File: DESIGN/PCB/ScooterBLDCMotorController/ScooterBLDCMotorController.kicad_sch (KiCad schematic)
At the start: 30 parts, among them J1 M1 OUTPUT, J10 RC_ENABLE, J2 M1 INPUT, J3 M2 INPUT, J4 M2 OUTPUT, J5 I2C, J6 TEST SWITCH, J7 RC CH 1, J8 RC CH 2, J9 RC_PWR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

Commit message: Latest PCB and Rev1.0 release
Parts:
- removed J2: M1 INPUT, Connector_JST:JST_XH_B3B-XH-A_1x03_P2.50mm_Vertical, symbol Connector_Generic:Conn_01x03
- removed J3: M2 INPUT, Connector_JST:JST_XH_B3B-XH-A_1x03_P2.50mm_Vertical, symbol Connector_Generic:Conn_01x03
- added J11: TO M2 ENCODER, Connector_JST:JST_XH_B5B-XH-A_1x05_P2.50mm_Vertical, symbol Connector_Generic:Conn_01x05
- added J12: M2 INPUT, Connector_JST:JST_XH_B5B-XH-A_1x05_P2.50mm_Vertical, symbol Connector_Generic:Conn_01x05
- added J2: TO M1 ENCODER, Connector_JST:JST_XH_B5B-XH-A_1x05_P2.50mm_Vertical, symbol Connector_Generic:Conn_01x05
- added J3: M1 INPUT, Connector_JST:JST_XH_B5B-XH-A_1x05_P2.50mm_Vertical, symbol Connector_Generic:Conn_01x05
- R1: footprint Resistor_THT:R_Axial_DIN0204_L3.6mm_D1.6mm_P5.08mm_Vertical -> Resistor_THT:R_Axial_DIN0204_L3.6mm_D1.6mm_P7.62mm_Horizontal
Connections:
- net M1 B: now also J2.3 (Pin_3), J3.3 (Pin_3)
- net M1 G: now also J2.4 (Pin_4), J3.4 (Pin_4)
- net M1 Y: now also J2.2 (Pin_2), J3.2 (Pin_2)
- net M2 B: now also J11.3 (Pin_3), J12.3 (Pin_3)
- net M2 G: now also J11.4 (Pin_4), J12.4 (Pin_4)
- net M2 Y: now also J11.2 (Pin_2), J12.2 (Pin_2)
- new net: J11.1 (Pin_1), J12.1 (Pin_1)
- new net: J11.5 (Pin_5), J12.5 (Pin_5)
- new net: J2.1 (Pin_1), J3.1 (Pin_1)
- new net: J2.5 (Pin_5), J3.5 (Pin_5)
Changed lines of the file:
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@@
   (junction (at 71.12 177.8) (diameter 0) (color 0 0 0 0)
   )
+  (junction (at 71.12 181.61) (diameter 0) (color 0 0 0 0)
+  )
   (junction (at 109.22 167.64) (diameter 0) (color 0 0 0 0)
   )
@@
   (junction (at 106.68 172.72) (diameter 0) (color 0 0 0 0)
   )
+  (junction (at 104.14 181.61) (diameter 0) (color 0 0 0 0)
+  )
+  (junction (at 73.66 181.61) (diameter 0) (color 0 0 0 0)
+  )
+  (junction (at 76.2 181.61) (diameter 0) (color 0 0 0 0)
+  )
   (junction (at 203.2 96.52) (diameter 0) (color 0 0 0 0)
   )
   (junction (at 104.14 177.8) (diameter 0) (color 0 0 0 0)
   )
+  (junction (at 106.68 181.61) (diameter 0) (color 0 0 0 0)
+  )
+  (junction (at 109.22 181.61) (diameter 0) (color 0 0 0 0)
+  )
   (wire (pts (xy 85.09 140.97) (xy 81.28 140.97))
     (stroke (width 0) (type default) (color 0 0 0 0))
@@
     (stroke (width 0) (type default) (color 0 0 0 0))
   )
+  (wire (pts (xy 109.22 181.61) (xy 109.22 189.23))
+    (stroke (width 0) (type default) (color 0 0 0 0))
+  )
   (wire (pts (xy 133.35 115.57) (xy 133.35 99.06))
     (stroke (width 0) (type default) (color 0 0 0 0))
@@
     (stroke (width 0) (type default) (color 0 0 0 0))
   )
+  (wire (pts (xy 78.74 181.61) (xy 78.74 189.23))
+    (stroke (width 0) (type default) (color 0 0 0 0))
+  )
   (wire (pts (xy 177.8 26.67) (xy 177.8 15.24))
     (stroke (width 0) (type default) (color 0 0 0 0))
@@
     (stroke (width 0) (type default) (color 0 0 0 0))
   )
+  (wire (pts (xy 71.12 181.61) (xy 71.12 189.23))
+    (stroke (width 0) (type default) (color 0 0 0 0))
+  )
   (wire (pts (xy 45.72 133.35) (xy 45.72 130.81))
     (stroke (width 0) (type default) (color 0 0 0 0))
@@
     (stroke (width 0) (type default) (color 0 0 0 0))
   )
+  (wire (pts (xy 101.6 181.61) (xy 101.6 189.23))
+    (stroke (width 0) (type default) (color 0 0 0 0))
+  )
   (wire (pts (xy 205.74 59.69) (xy 190.5 59.69))
     (stroke (width 0) (type default) (color 0 0 0 0))
@@
     (stroke (width 0) (type default) (color 0 0 0 0))
   )
+  (wire (pts (xy 111.76 181.61) (xy 111.76 189.23))
+    (stroke (width 0) (type default) (color 0 0 0 0))
+  )
   (wire (pts (xy 69.85 83.82) (xy 69.85 88.9))
     (stroke (width 0) (type default) (color 0 0 0 0))
@@
     (stroke (width 0) (type default) (color 0 0 0 0))
   )
+  (wire (pts (xy 73.66 181.61) (xy 73.66 189.23))
+    (stroke (width 0) (type default) (color 0 0 0 0))
+  )
   (wire (pts (xy 113.03 154.94) (xy 113.03 162.56))
     (stroke (width 0) (type default) (color 0 0 0 0))
@@
     (stroke (width 0) (type default) (color 0 0 0 0))
   )
+  (wire (pts (xy 104.14 181.61) (xy 104.14 189.23))
+    (stroke (width 0) (type default) (color 0 0 0 0))
+  )
   (wire (pts (xy 90.17 130.81) (xy 90.17 133.35))
     (stroke (width 0) (type default) (color 0 0 0 0))
@@
     (stroke (width 0) (type default) (color 0 0 0 0))
   )
+  (wire (pts (xy 68.58 181.61) (xy 68.58 189.23))
+    (stroke (width 0) (type default) (color 0 0 0 0))
+  )
   (wire (pts (xy 97.79 106.68) (xy 85.09 106.68))
     (stroke (width 0) (type default) (color 0 0 0 0))
@@
     (stroke (width 0) (type default) (color 0 0 0 0))
   )
+  (wire (pts (xy 106.68 181.61) (xy 106.68 189.23))
+    (stroke (width 0) (type default) (color 0 0 0 0))
+  )
   (wire (pts (xy 248.92 54.61) (xy 240.03 54.61))
     (stroke (width 0) (type default) (color 0 0 0 0))
@@
   )
   (wire (pts (xy 245.11 44.45) (xy 252.73 44.45))
+    (stroke (width 0) (type default) (color 0 0 0 0))
+  )
+  (wire (pts (xy 76.2 181.61) (xy 76.2 189.23))
     (stroke (width 0) (type default) (color 0 0 0 0))
   )
@@
     (pin "9")
   )
+  (symbol (lib_id "Connector_Generic:Conn_01x05") (at 106.68 194.31 270) (unit 1)
+    (in_bom yes) (on_board yes)
+    (property "Reference" "J12" (id 0) (at 115.57 191.77 90))
+    (property "Value" "M2 INPUT" (id 1) (at 119.38 194.31 90))
+    (property "Footprint" "Connector_JST:JST_XH_B5B-XH-A_1x05_P2.50mm_Vertical" (id 2) (at 106.68 194.31 0)
+      (effects (font (size 1.27 1.27)) hide)
+    )
+    (property "Datasheet" "~" (id 3) (at 106.68 194.31 0)
+      (effects (font (size 1.27 1.27)) hide)
+    )
+    (pin "1")
+    (pin "2")
+    (pin "3")
+    (pin "4")
+    (pin "5")
+  )
+  (symbol (lib_id "Connector_Generic:Conn_01x05") (at 73.66 186.69 270) (unit 1)
+    (in_bom yes) (on_board yes)
+    (property "Reference" "J2" (id 0) (at 82.55 184.15 90))
+    (property "Value" "TO M1 ENCODER" (id 1) (at 88.9 186.69 90))
+    (property "Footprint" "Connector_JST:JST_XH_B5B-XH-A_1x05_P2.50mm_Vertical" (id 2) (at 73.66 186.69 0)
+      (effects (font (size 1.27 1.27)) hide)
+    )
+    (property "Datasheet" "~" (id 3) (at 73.66 186.69 0)
+      (effects (font (size 1.27 1.27)) hide)
+    )
+    (pin "1")
+    (pin "2")
+    (pin "3")
+    (pin "4")
+    (pin "5")
+  )
   (symbol (lib_id "Custom:Level_Shifter") (at 171.45 34.29 90) (unit 1)
     (in_bom yes) (on_board yes) (fields_autoplaced)
@@
     (property "Reference" "R1" (id 0) (at 193.04 99.06 90))
     (property "Value" "R" (id 1) (at 193.04 96.52 90))
-    (property "Footprint" "Resistor_THT:R_Axial_DIN0204_L3.6mm_D1.6mm_P5.08mm_Vertical" (id 2) (at 193.04 98.298 90)
+    (property "Footprint" "Resistor_THT:R_Axial_DIN0204_L3.6mm_D1.6mm_P7.62mm_Horizontal" (id 2) (at 193.04 98.298 90)
       (effects (font (size 1.27 1.27)) hide)
     )
@@
     (pin "4")
   )
-  (symbol (lib_id "Connector_Generic:Conn_01x03") (at 106.68 186.69 270) (unit 1)
-    (in_bom yes) (on_board yes)
-    (property "Reference" "J3" (id 0) (at 111.76 185.4199 90)
-      (effects (font (size 1.27 1.27)) (justify left))
-    )
-    (property "Value" "M2 INPUT" (id 1) (at 102.87 190.5 90)
-      (effects (font (size 1.27 1.27)) (justify left))
-    )
-    (property "Footprint" "Connector_JST:JST_XH_B3B-XH-A_1x03_P2.50mm_Vertical" (id 2) (at 106.68 186.69 0)
+  (symbol (lib_id "Connector_Generic:Conn_01x05") (at 106.68 186.69 270) (unit 1)
+    (in_bom yes) (on_board yes)
+    (property "Reference" "J11" (id 0) (at 115.57 184.15 90))
+    (property "Value" "TO M2 ENCODER" (id 1) (at 121.92 186.69 90))
+    (property "Footprint" "Connector_JST:JST_XH_B5B-XH-A_1x05_P2.50mm_Vertical" (id 2) (at 106.68 186.69 0)
       (effects (font (size 1.27 1.27)) hide)
     )
@@
     (pin "2")
     (pin "3")
+    (pin "4")
+    (pin "5")
   )
   (symbol (lib_id "Custom:SN74HC14NR") (at 107.95 151.13 270) (unit 1)
@@
     (pin "9")
   )
+  (symbol (lib_id "Connector_Generic:Conn_01x05") (at 73.66 194.31 270) (unit 1)
+    (in_bom yes) (on_board yes)
+    (property "Reference" "J3" (id 0) (at 82.55 191.77 90))
+    (property "Value" "M1 INPUT" (id 1) (at 86.36 194.31 90))
+    (property "Footprint" "Connector_JST:JST_XH_B5B-XH-A_1x05_P2.50mm_Vertical" (id 2) (at 73.66 194.31 0)
+      (effects (font (size 1.27 1.27)) hide)
+    )
+    (property "Datasheet" "~" (id 3) (at 73.66 194.31 0)
+      (effects (font (size 1.27 1.27)) hide)
+    )
+    (pin "1")
+    (pin "2")
+    (pin "3")
+    (pin "4")
+    (pin "5")
+  )
   (symbol (lib_id "Device:C") (at 116.84 172.72 270) (unit 1)
     (in_bom yes) (on_board yes)
@@
     (pin "1")
     (pin "2")
-  )
-  (symbol (lib_id "Connector_Generic:Conn_01x03") (at 73.66 186.69 270) (unit 1)
-    (in_bom yes) (on_board yes)
-    (property "Reference" "J2" (id 0) (at 78.74 185.4199 90)
-      (effects (font (size 1.27 1.27)) (justify left))
-    )
-    (property "Value" "M1 INPUT" (id 1) (at 69.85 190.5 90)
-      (effects (font (size 1.27 1.27)) (justify left))
-    )
-    (property "Footprint" "Connector_JST:JST_XH_B3B-XH-A_1x03_P2.50mm_Vertical" (id 2) (at 73.66 186.69 0)
-      (effects (font (size 1.27 1.27)) hide)
-    )
-    (property "Datasheet" "~" (id 3) (at 73.66 186.69 0)
-      (effects (font (size 1.27 1.27)) hide)
-    )
-    (pin "1")
-    (pin "2")
-    (pin "3")
   )
   (symbol (lib_id "Custom:3.3V_Voltage_Regulator") (at 252.73 40.64 90) (unit 1)
@@
       (reference "J1") (unit 1) (value "M1 OUTPUT") (footprint "Connector_JST:JST_XH_B3B-XH-A_1x03_P2.50mm_Vertical")
     )
-    (path "/c803ae01-d083-4855-8801-39dea92f7d1b"
-      (reference "J2") (unit 1) (value "M1 INPUT") (footprint "Connector_JST:JST_XH_B3B-XH-A_1x03_P2.50mm_Vertical")
-    )
-    (path "/9925a326-63ef-4346-b01c-a42c2e49fa06"
-      (reference "J3") (unit 1) (value "M2 INPUT") (footprint "Connector_JST:JST_XH_B3B-XH-A_1x03_P2.50mm_Vertical")
+    (path "/6c578b81-c5ac-40f2-828f-f316ca08e2c9"
+      (reference "J2") (unit 1) (value "TO M1 ENCODER") (footprint "Connector_JST:JST_XH_B5B-XH-A_1x05_P2.50mm_Vertical")
+    )
+    (path "/a535aaee-d403-444b-bf48-91bd8f6bbbbb"
+      (reference "J3") (unit 1) (value "M1 INPUT") (footprint "Connector_JST:JST_XH_B5B-XH-A_1x05_P2.50mm_Vertical")
     )
     (path "/18022ffe-56bf-49ac-890a-29ec31eec758"
@@
       (reference "J10") (unit 1) (value "RC_ENABLE") (footprint "Connector_PinHeader_2.54mm:PinHeader_1x02_P2.54mm_Vertical")
     )
+    (path "/9c217da1-3f00-4b6e-8b3e-d4724992586b"
+      (reference "J11") (unit 1) (value "TO M2 ENCODER") (footprint "Connector_JST:JST_XH_B5B-XH-A_1x05_P2.50mm_Vertical")
+    )
+    (path "/4811cedc-e653-4dd3-ab03-bd6ac45aea2a"
+      (reference "J12") (unit 1) (value "M2 INPUT") (footprint "Connector_JST:JST_XH_B5B-XH-A_1x05_P2.50mm_Vertical")
+    )
     (path "/121b8a59-e57c-4cdd-877c-c2b279b4ad3b"
       (reference "POWER1") (unit 1) (value "5v") (footprint "Connector_JST:JST_XH_B2B-XH-A_1x02_P2.50mm_Vertical")
     )
     (path "/8811b52e-d3c2-4783-979a-166200d19a26"
-      (reference "R1") (unit 1) (value "R") (footprint "Resistor_THT:R_Axial_DIN0204_L3.6mm_D1.6mm_P5.08mm_Vertical")
+      (reference "R1") (unit 1) (value "R") (footprint "Resistor_THT:R_Axial_DIN0204_L3.6mm_D1.6mm_P7.62mm_Horizontal")
     )
     (path "/a906d8c4-7ffd-463c-a1b9-091846f7101c"

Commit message: Fixed swapped connections on level shifter.
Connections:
- net 3v: now also U1.9 (LV), U10.9 (LV), U3.9 (LV), U6.9 (LV); no longer U1.10 (LV), U10.10 (LV), U3.10 (LV), U6.10 (LV)
- net GND: now also U1.10 (GND), U10.10 (GND), U3.10 (GND), U6.10 (GND); no longer U1.9 (GND), U10.9 (GND), U3.9 (GND), U6.9 (GND)
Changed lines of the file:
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@@
     (pin "3")
   )
-  (symbol (lib_id "Custom:Level_Shifter") (at 93.98 123.19 90) (unit 1)
+  (symbol (lib_name "Level_Shifter_2") (lib_id "Custom:Level_Shifter") (at 93.98 123.19 90) (unit 1)
     (in_bom yes) (on_board yes) (fields_autoplaced)
     (property "Reference" "U3" (id 0) (at 102.87 121.9199 90)
@@
     (pin "5")
   )
-  (symbol (lib_id "Custom:Level_Shifter") (at 171.45 34.29 90) (unit 1)
+  (symbol (lib_name "Level_Shifter_3") (lib_id "Custom:Level_Shifter") (at 171.45 34.29 90) (unit 1)
     (in_bom yes) (on_board yes) (fields_autoplaced)
     (property "Reference" "U10" (id 0) (at 180.34 33.0199 90)
@@
     (pin "2")
   )
-  (symbol (lib_id "Custom:Level_Shifter") (at 46.99 123.19 90) (unit 1)
+  (symbol (lib_name "Level_Shifter_1") (lib_id "Custom:Level_Shifter") (at 46.99 123.19 90) (unit 1)
     (in_bom yes) (on_board yes)
     (property "Reference" "U1" (id 0) (at 57.15 121.92 90))

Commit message: Revision 1.2 of MotorController board
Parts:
- removed U7: 5V_Voltage_Regulator, Custom:Voltage Regulator, symbol Custom:5V_Voltage_Regulator
- removed U8: 3.3V_Voltage_Regulator, Custom:Voltage Regulator, symbol Custom:3.3V_Voltage_Regulator
- removed U9: (no value), Custom:I2C Level Shifter, symbol Custom:I2C_Level_Shifter
- added J13, J14: Conn_01x01_Male, Connector_PinHeader_2.54mm:PinHeader_1x01_P2.54mm_Vertical, symbol Connector:Conn_01x01_Male
- added U7: (no value), Custom:Level Shifter, symbol Custom:Level_Shifter
- added U8: 5V_StepUpDown_Voltage_Regulator, Custom:StepUpDown Voltage Regulator, symbol Custom:5V_StepUpDown_Voltage_Regulator
- added U9: 3V_StepUpDown_Voltage_Regulator, Custom:StepUpDown Voltage Regulator, symbol Custom:3V_StepUpDown_Voltage_Regulator
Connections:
- net 3v: now also U7.9 (LV), U9.3 (VOUT), U9.4 (~{SHDN})
- net 5v: now also U7.4 (HV), U8.3 (VOUT), U8.4 (~{SHDN}), U9.1 (VIN)
- net GND: now also J13.1 (Pin_1), J14.1 (Pin_1), U7.10 (GND), U7.3 (GND), U8.2 (GND), U9.2 (GND)
- net at D1.1 (K): now also U8.1 (VIN)
- net at J5.1 (Pin_1): now also U7.6 (HV1)
- net at J5.2 (Pin_2): now also U7.5 (HV2)
- net at U4.23 (16_A2_RX4_SCL1): now also U7.8 (LV2)
- net at U4.24 (17_A3_TX4_SDA1): now also U7.7 (LV1)
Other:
- moved on the sheet: J5

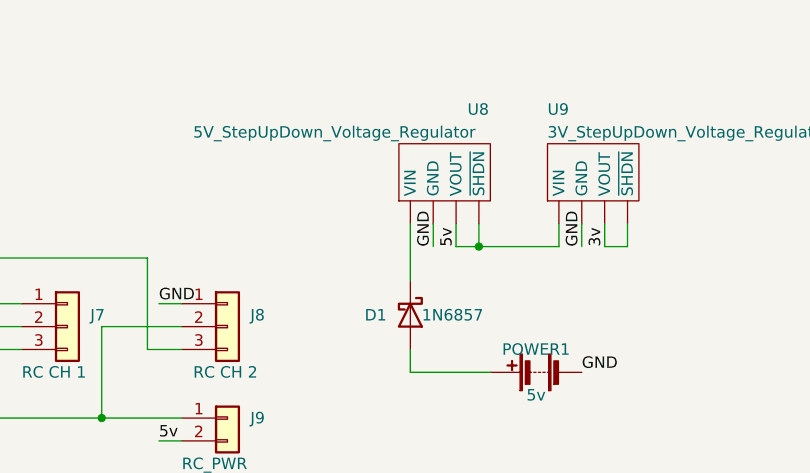
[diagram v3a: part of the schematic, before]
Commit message: Updated PCB to use terminals, added new DriveByRC code
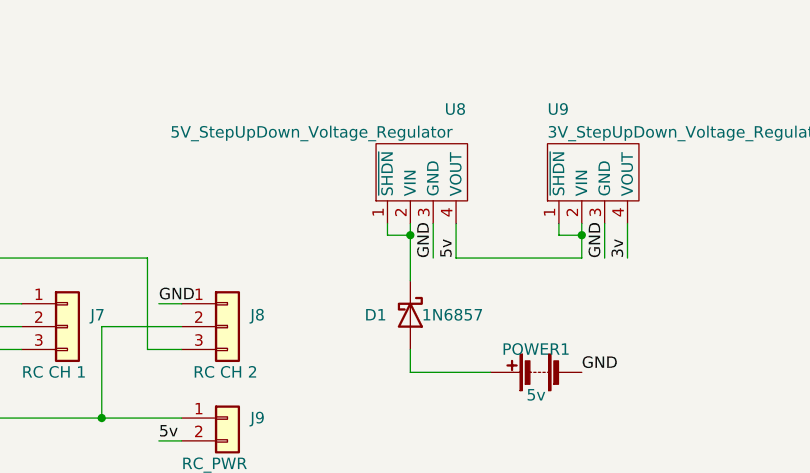
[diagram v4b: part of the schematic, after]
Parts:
- J1, J4: footprint Connector_JST:JST_XH_B3B-XH-A_1x03_P2.50mm_Vertical -> TerminalBlock:TerminalBlock_Altech_AK300-3_P5.00mm
- J12, J3: footprint Connector_JST:JST_XH_B5B-XH-A_1x05_P2.50mm_Vertical -> Custom:TerminalBlock_Altech_AK300-5_P5.00mm
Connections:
- net 3v: no longer U9.3 (VOUT)
- net 5v: now also U9.2 (VIN); no longer U8.3 (VOUT)
- net GND: now also U8.3 (GND), U9.3 (GND); no longer U8.2 (GND), U9.2 (GND)
- net at D1.1 (K), U8.1 (~{SHDN}): now also U8.2 (VIN)

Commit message: Revision 1.3 for PCB
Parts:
- added J15: RC CH 3, Connector_JST:JST_XH_B3B-XH-A_1x03_P2.50mm_Vertical, symbol Connector_Generic:Conn_01x03
- added R2, R3: R, Resistor_THT:R_Axial_DIN0204_L3.6mm_D1.6mm_P7.62mm_Horizontal, symbol Device:R
- C1, C2, C3, C4, C5, C6, D1, J13, J14, R1, U1, U10, U3, U4, U6, U7, U8, U9: now left out of the parts list
- J1, J4: LCSC (none) -> C8393
- J10, J9: LCSC (none) -> C5116481
- J11, J2: LCSC (none) -> C157991
- J12, J3: LCSC (none) -> C395854
- J5, J6, POWER1, SERIAL1: LCSC (none) -> C158012
- J7, J8: LCSC (none) -> C161870
- U2, U5: LCSC (none) -> C2907
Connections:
- net 3v: now also R2.2, R3.2
- net GND: now also J15.1 (Pin_1)
- net at J7.2 (Pin_2), J8.2 (Pin_2), J9.1 (Pin_1): now also J15.2 (Pin_2)
- net at J5.1 (Pin_1): now also U4.23 (16_A2_RX4_SCL1), R2.1; no longer U7.6 (HV1)
- net at J5.2 (Pin_2): now also U4.24 (17_A3_TX4_SDA1), R3.1; no longer U7.5 (HV2)
- net at U7.8 (LV2): no longer U4.23 (16_A2_RX4_SCL1)
- net at U7.7 (LV1): now also U4.26 (19_A5_SCL0); no longer U4.24 (17_A3_TX4_SDA1)
- new net: J15.3 (Pin_3), U7.6 (HV1)
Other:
- moved on the sheet: D1, J13, J14, J5, POWER1, U8, U9
